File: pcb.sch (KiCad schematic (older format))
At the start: 1 part, among them U1 STM32F103C8Tx

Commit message: added correct MCU footprint and symbol
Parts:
- removed U1: STM32F103C8Tx, Package_QFP:LQFP-48_7x7mm_P0.5mm, symbol MCU_ST_STM32F1:STM32F103C8Tx
- added U1: STM32F103C8T6, STM32F103C8T6:QFP50P900X900X160-48N, symbol STM32F103C8T6:STM32F103C8T6
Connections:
- net labels added: +3.3VA, +3V3, GND, GNDA
- wire segments 0 -> 12
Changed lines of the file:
@@
 $EndDescr
 $Comp
-L MCU_ST_STM32F1:STM32F103C8Tx U1
-U 1 1 620F1E41
-P 6650 4100
-F 0 "U1" H 6600 2511 50  0000 C CNN
-F 1 "STM32F103C8Tx" H 6600 2420 50  0000 C CNN
-F 2 "Package_QFP:LQFP-48_7x7mm_P0.5mm" H 6050 2700 50  0001 R CNN
-F 3 "http://www.st.com/st-web-ui/static/active/en/resource/technical/document/datasheet/CD00161566.pdf" H 6650 4100 50  0001 C CNN
-	1    6650 4100
+L STM32F103C8T6:STM32F103C8T6 U1
+U 1 1 62107107
+P 7000 4600
+F 0 "U1" H 7000 6367 50  0000 C CNN
+F 1 "STM32F103C8T6" H 7000 6276 50  0000 C CNN
+F 2 "STM32F103C8T6:QFP50P900X900X160-48N" H 7000 4600 50  0001 L BNN
+F 3 "" H 7000 4600 50  0001 L BNN
+F 4 "10" H 7000 4600 50  0001 L BNN "PARTREV"
+F 5 "IPC7351B" H 7000 4600 50  0001 L BNN "STANDARD"
+F 6 "ST Microelectronics" H 7000 4600 50  0001 L BNN "MANUFACTURER"
+	1    7000 4600
 	1    0    0    -1
 $EndComp
+$Comp
+L power:+3V3 #PWR?
+U 1 1 6210956F
+P 8250 3000
+F 0 "#PWR?" H 8250 2850 50  0001 C CNN
+F 1 "+3V3" H 8265 3173 50  0000 C CNN
+F 2 "" H 8250 3000 50  0001 C CNN
+F 3 "" H 8250 3000 50  0001 C CNN
+	1    8250 3000
+	1    0    0    -1
+$EndComp
+Wire Wire Line
+	8250 3000 8250 3200
+Wire Wire Line
+	8250 3200 8000 3200
+$Comp
+L power:+3.3VA #PWR?
+U 1 1 6210AEB8
+P 8000 3000
+F 0 "#PWR?" H 8000 2850 50  0001 C CNN
+F 1 "+3.3VA" H 8015 3173 50  0000 C CNN
+F 2 "" H 8000 3000 50  0001 C CNN
+F 3 "" H 8000 3000 50  0001 C CNN
+	1    8000 3000
+	1    0    0    -1
+$EndComp
+Wire Wire Line
+	8000 3000 8000 3100
+$Comp
+L power:GND #PWR?
+U 1 1 6210B942
+P 8200 6050
+F 0 "#PWR?" H 8200 5800 50  0001 C CNN
+F 1 "GND" H 8205 5877 50  0000 C CNN
+F 2 "" H 8200 6050 50  0001 C CNN
+F 3 "" H 8200 6050 50  0001 C CNN
+	1    8200 6050
+	1    0    0    -1
+$EndComp
+$Comp
+L power:GNDA #PWR?
+U 1 1 6210C0B9
+P 8400 6050
+F 0 "#PWR?" H 8400 5800 50  0001 C CNN
+F 1 "GNDA" H 8405 5877 50  0000 C CNN
+F 2 "" H 8400 6050 50  0001 C CNN
+F 3 "" H 8400 6050 50  0001 C CNN
+	1    8400 6050
+	1    0    0    -1
+$EndComp
+Wire Wire Line
+	8200 6050 8200 6000
+Wire Wire Line
+	8200 6000 8000 6000
+Wire Wire Line
+	8400 6050 8400 5900
+Wire Wire Line
+	8400 5900 8000 5900
+Wire Wire Line
+	8250 3200 8500 3200
+Wire Wire Line
+	8500 3200 8500 2750
+Wire Wire Line
+	8500 2750 5950 2750
+Wire Wire Line
+	5950 2750 5950 3400
+Wire Wire Line
+	5950 3400 6000 3400
+Connection ~ 8250 3200
 $EndSCHEMATC

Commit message: created footprints and symbols for gps, compass and encoder
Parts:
- added G1: GPS_NEO_6M_module, components_ece445:GPS_NEO_6M_module, symbol components_senior_design:GPS_NEO_6M_module
- added U2: Shaft_encoder, components_ece445:shaft_encoder, symbol components_senior_design:Shaft_encoder
- added U3: compass_accelerometer, components_ece445:compass_accelerometer, symbol components_senior_design:compass_accelerometer
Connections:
- net labels added: +5V
- net labels removed: +3.3VA, GNDA
- wire segments 12 -> 22
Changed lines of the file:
@@
 $EndDescr
+$Comp
+L power:+3V3 #PWR03
+U 1 1 6210956F
+P 8250 3000
+F 0 "#PWR03" H 8250 2850 50  0001 C CNN
+F 1 "+3V3" H 8265 3173 50  0000 C CNN
+F 2 "" H 8250 3000 50  0001 C CNN
+F 3 "" H 8250 3000 50  0001 C CNN
+	1    8250 3000
+	1    0    0    -1
+$EndComp
+Wire Wire Line
+	8250 3000 8250 3200
+$Comp
+L power:GND #PWR02
+U 1 1 6210B942
+P 8200 6050
+F 0 "#PWR02" H 8200 5800 50  0001 C CNN
+F 1 "GND" H 8205 5877 50  0000 C CNN
+F 2 "" H 8200 6050 50  0001 C CNN
+F 3 "" H 8200 6050 50  0001 C CNN
+	1    8200 6050
+	1    0    0    -1
+$EndComp
+Wire Wire Line
+	8200 6050 8200 6000
+Wire Wire Line
+	8250 3200 8500 3200
+Wire Wire Line
+	8500 3200 8500 2750
+Wire Wire Line
+	8500 2750 5950 2750
+Wire Wire Line
+	5950 2750 5950 3400
+Wire Wire Line
+	5950 3400 6000 3400
+Connection ~ 8250 3200
+Wire Wire Line
+	8200 6000 8000 6000
 $Comp
 L STM32F103C8T6:STM32F103C8T6 U1
@@
 	1    0    0    -1
 $EndComp
+Wire Wire Line
+	8200 6000 8200 5900
+Connection ~ 8200 6000
+Wire Wire Line
+	8200 5900 8000 5900
 $Comp
-L power:+3V3 #PWR?
-U 1 1 6210956F
-P 8250 3000
-F 0 "#PWR?" H 8250 2850 50  0001 C CNN
-F 1 "+3V3" H 8265 3173 50  0000 C CNN
-F 2 "" H 8250 3000 50  0001 C CNN
-F 3 "" H 8250 3000 50  0001 C CNN
-	1    8250 3000
+L power:+3V3 #PWR0101
+U 1 1 6211EE7A
+P 3750 1750
+F 0 "#PWR0101" H 3750 1600 50  0001 C CNN
+F 1 "+3V3" H 3765 1923 50  0000 C CNN
+F 2 "" H 3750 1750 50  0001 C CNN
+F 3 "" H 3750 1750 50  0001 C CNN
+	1    3750 1750
+	1    0    0    -1
+$EndComp
+$Comp
+L power:GND #PWR0102
+U 1 1 6211F78C
+P 3750 2200
+F 0 "#PWR0102" H 3750 1950 50  0001 C CNN
+F 1 "GND" H 3755 2027 50  0000 C CNN
+F 2 "" H 3750 2200 50  0001 C CNN
+F 3 "" H 3750 2200 50  0001 C CNN
+	1    3750 2200
 	1    0    0    -1
 $EndComp
 Wire Wire Line
-	8250 3000 8250 3200
+	3400 2150 3750 2150
 Wire Wire Line
-	8250 3200 8000 3200
+	3750 2150 3750 2200
+Wire Wire Line
+	3400 1850 3750 1850
+Wire Wire Line
+	3750 1850 3750 1750
+Wire Wire Line
+	8000 3200 8100 3200
+Wire Wire Line
+	8000 3100 8100 3100
+Wire Wire Line
+	8100 3100 8100 3200
+Connection ~ 8100 3200
+Wire Wire Line
+	8100 3200 8250 3200
 $Comp
-L power:+3.3VA #PWR?
-U 1 1 6210AEB8
-P 8000 3000
-F 0 "#PWR?" H 8000 2850 50  0001 C CNN
-F 1 "+3.3VA" H 8015 3173 50  0000 C CNN
-F 2 "" H 8000 3000 50  0001 C CNN
-F 3 "" H 8000 3000 50  0001 C CNN
-	1    8000 3000
+L components_senior_design:GPS_NEO_6M_module G1
+U 1 1 621243D2
+P 3150 1900
+F 0 "G1" H 3208 2175 50  0000 C CNN
+F 1 "GPS_NEO_6M_module" H 3208 2084 50  0000 C CNN
+F 2 "components_ece445:GPS_NEO_6M_module" H 3150 1500 50  0001 C CNN
+F 3 "" H 3200 1950 50  0001 C CNN
+	1    3150 1900
+	1    0    0    -1
+$EndComp
+$Comp
+L components_senior_design:Shaft_encoder U2
+U 1 1 621258F0
+P 3150 2750
+F 0 "U2" H 3208 2975 50  0000 C CNN
+F 1 "Shaft_encoder" H 3208 2884 50  0000 C CNN
+F 2 "components_ece445:shaft_encoder" H 3200 2400 50  0001 C CNN
+F 3 "" H 3150 2950 50  0001 C CNN
+	1    3150 2750
+	1    0    0    -1
+$EndComp
+$Comp
+L power:+5V #PWR0103
+U 1 1 6212655A
+P 3650 2650
+F 0 "#PWR0103" H 3650 2500 50  0001 C CNN
+F 1 "+5V" H 3665 2823 50  0000 C CNN
+F 2 "" H 3650 2650 50  0001 C CNN
+F 3 "" H 3650 2650 50  0001 C CNN
+	1    3650 2650
 	1    0    0    -1
 $EndComp
 Wire Wire Line
-	8000 3000 8000 3100
+	3650 2650 3650 2750
+Wire Wire Line
+	3650 2750 3450 2750
 $Comp
-L power:GND #PWR?
-U 1 1 6210B942
-P 8200 6050
-F 0 "#PWR?" H 8200 5800 50  0001 C CNN
-F 1 "GND" H 8205 5877 50  0000 C CNN
-F 2 "" H 8200 6050 50  0001 C CNN
-F 3 "" H 8200 6050 50  0001 C CNN
-	1    8200 6050
-	1    0    0    -1
-$EndComp
-$Comp
-L power:GNDA #PWR?
-U 1 1 6210C0B9
-P 8400 6050
-F 0 "#PWR?" H 8400 5800 50  0001 C CNN
-F 1 "GNDA" H 8405 5877 50  0000 C CNN
-F 2 "" H 8400 6050 50  0001 C CNN
-F 3 "" H 8400 6050 50  0001 C CNN
-	1    8400 6050
+L power:GND #PWR0104
+U 1 1 62127216
+P 3650 3000
+F 0 "#PWR0104" H 3650 2750 50  0001 C CNN
+F 1 "GND" H 3655 2827 50  0000 C CNN
+F 2 "" H 3650 3000 50  0001 C CNN
+F 3 "" H 3650 3000 50  0001 C CNN
+	1    3650 3000
 	1    0    0    -1
 $EndComp
 Wire Wire Line
-	8200 6050 8200 6000
+	3450 2950 3650 2950
 Wire Wire Line
-	8200 6000 8000 6000
-Wire Wire Line
-	8400 6050 8400 5900
-Wire Wire Line
-	8400 5900 8000 5900
-Wire Wire Line
-	8250 3200 8500 3200
-Wire Wire Line
-	8500 3200 8500 2750
-Wire Wire Line
-	8500 2750 5950 2750
-Wire Wire Line
-	5950 2750 5950 3400
-Wire Wire Line
-	5950 3400 6000 3400
-Connection ~ 8250 3200
+	3650 2950 3650 3000
+$Comp
+L components_senior_design:compass_accelerometer U3
+U 1 1 6212A98F
+P 3200 3500
+F 0 "U3" H 3233 3715 50  0000 C CNN
+F 1 "compass_accelerometer" H 3233 3624 50  0000 C CNN
+F 2 "components_ece445:compass_accelerometer" H 3250 2550 50  0001 C CNN
+F 3 "" H 3200 3700 50  0001 C CNN
+	1    3200 3500
+	1    0    0    -1
+$EndComp
 $EndSCHEMATC

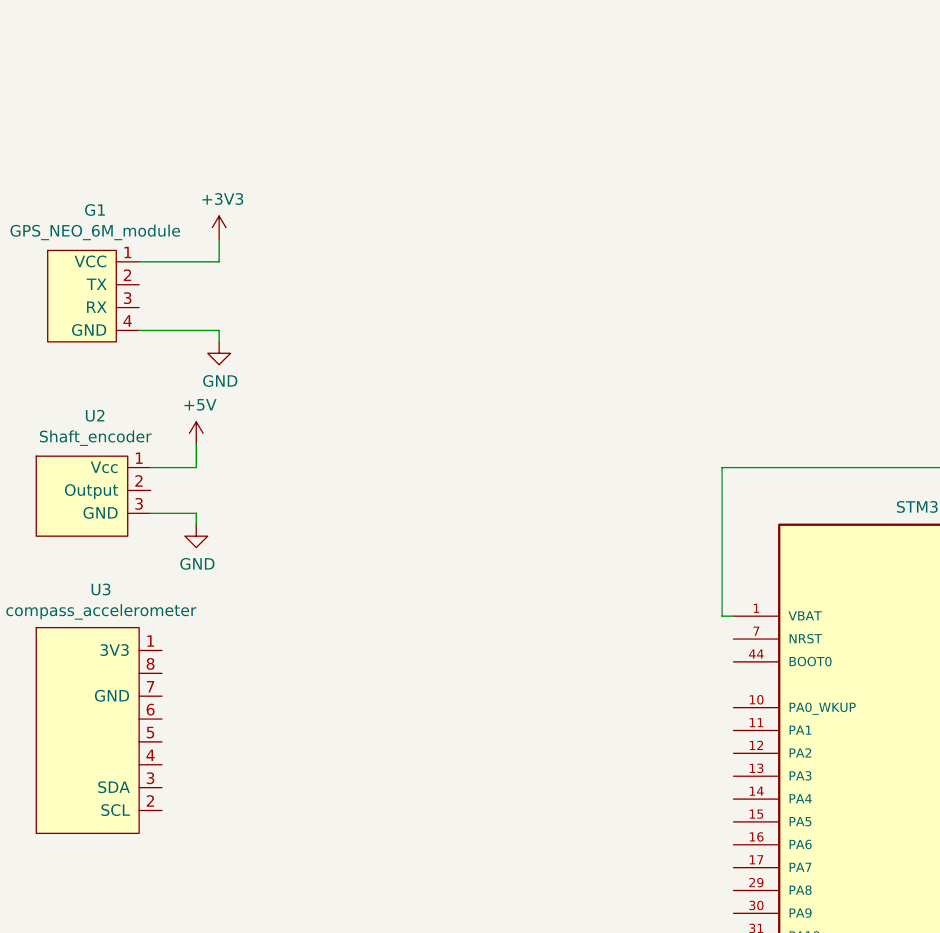
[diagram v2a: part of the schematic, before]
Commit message: added 3V7 to 3V3 convertor
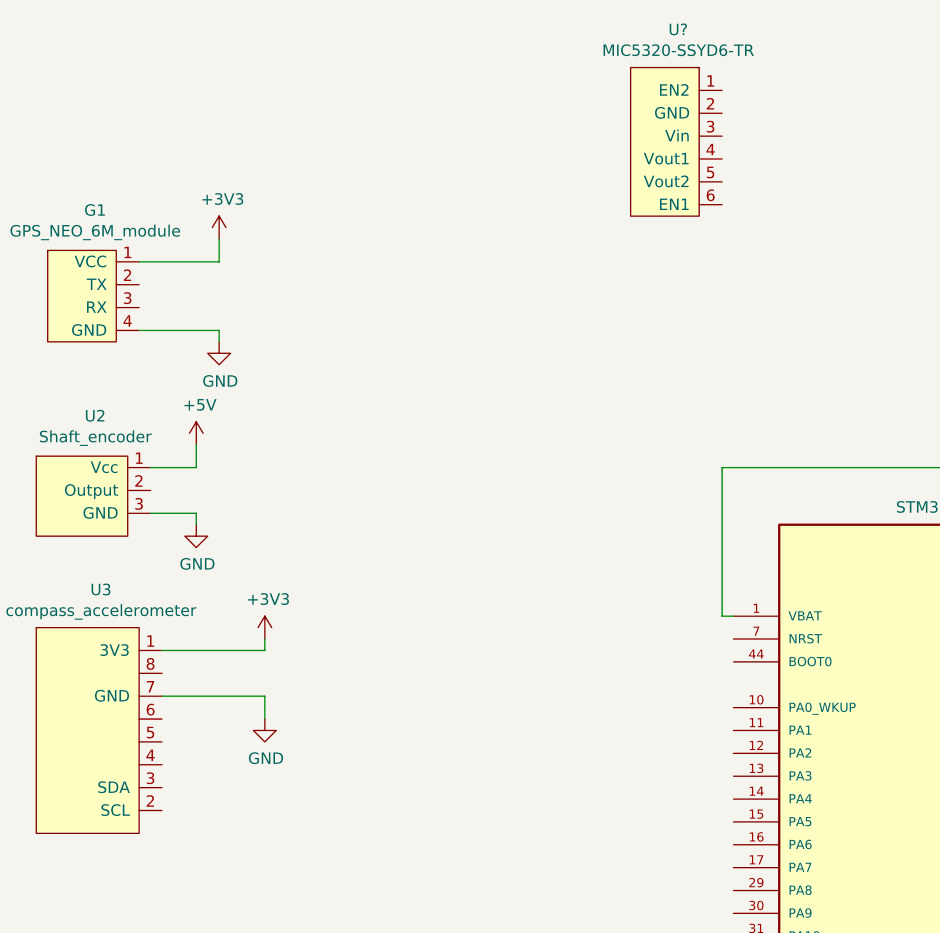
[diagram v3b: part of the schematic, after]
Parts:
- added U?: MIC5320-SSYD6-TR, MIC5320-SSYD6-TR:SOT95P280X110-6N, symbol components_senior_design:MIC5320-SSYD6-TR
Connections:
- net +3V3: now also U3.1 (3V3)
- net GND: now also U3.7 (GND)
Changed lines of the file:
@@
+	1    0    0    -1
+$EndComp
+$Comp
+L power:+3V3 #PWR0105
+U 1 1 6212C9CF
+P 3950 3500
+F 0 "#PWR0105" H 3950 3350 50  0001 C CNN
+F 1 "+3V3" H 3965 3673 50  0000 C CNN
+F 2 "" H 3950 3500 50  0001 C CNN
+F 3 "" H 3950 3500 50  0001 C CNN
+	1    3950 3500
+	1    0    0    -1
+$EndComp
+Wire Wire Line
+	3500 3550 3950 3550
+Wire Wire Line
+	3950 3550 3950 3500
+$Comp
+L power:GND #PWR0106
+U 1 1 6212D678
+P 3950 3850
+F 0 "#PWR0106" H 3950 3600 50  0001 C CNN
+F 1 "GND" H 3955 3677 50  0000 C CNN
+F 2 "" H 3950 3850 50  0001 C CNN
+F 3 "" H 3950 3850 50  0001 C CNN
+	1    3950 3850
+	1    0    0    -1
+$EndComp
+Wire Wire Line
+	3500 3750 3950 3750
+Wire Wire Line
+	3950 3750 3950 3850
+$Comp
+L components_senior_design:MIC5320-SSYD6-TR U?
+U 1 1 6213371B
+P 5750 1250
+F 0 "U?" H 5758 1665 50  0000 C CNN
+F 1 "MIC5320-SSYD6-TR" H 5758 1574 50  0000 C CNN
+F 2 "MIC5320-SSYD6-TR:SOT95P280X110-6N" H 5800 750 50  0001 C CNN
+F 3 "" H 5750 1200 50  0001 C CNN
+	1    5750 1250
 	1    0    0    -1
 $EndComp

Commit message: finished power supply
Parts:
- added C1, C2: 1uF, symbol device:C
- added J1: Conn_01x02, symbol Connector_Generic:Conn_01x02
- added U5: 3v7_to_5V_boost, components_ece445:3v7_to_5V_boost, symbol components_senior_design:3v7_to_5V_boost
- gave numbers to parts that had none: 1
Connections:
- net +3V3: now also U4.4 (Vout1), U4.5 (Vout2), C2.1
- net +5V: now also U4.1 (EN2), U4.3 (Vin), U4.6 (EN1), C1.1, U5.6 (Vout)
- net GND: now also U4.2 (GND), C1.2, C2.2, J1.2 (Pin_2), U5.3 (GND), U5.5 (GND)
- new net +3V8: J1.1 (Pin_1), U5.4 (Vbat)
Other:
- moved on the sheet: G1, U1, U2, U3, U4

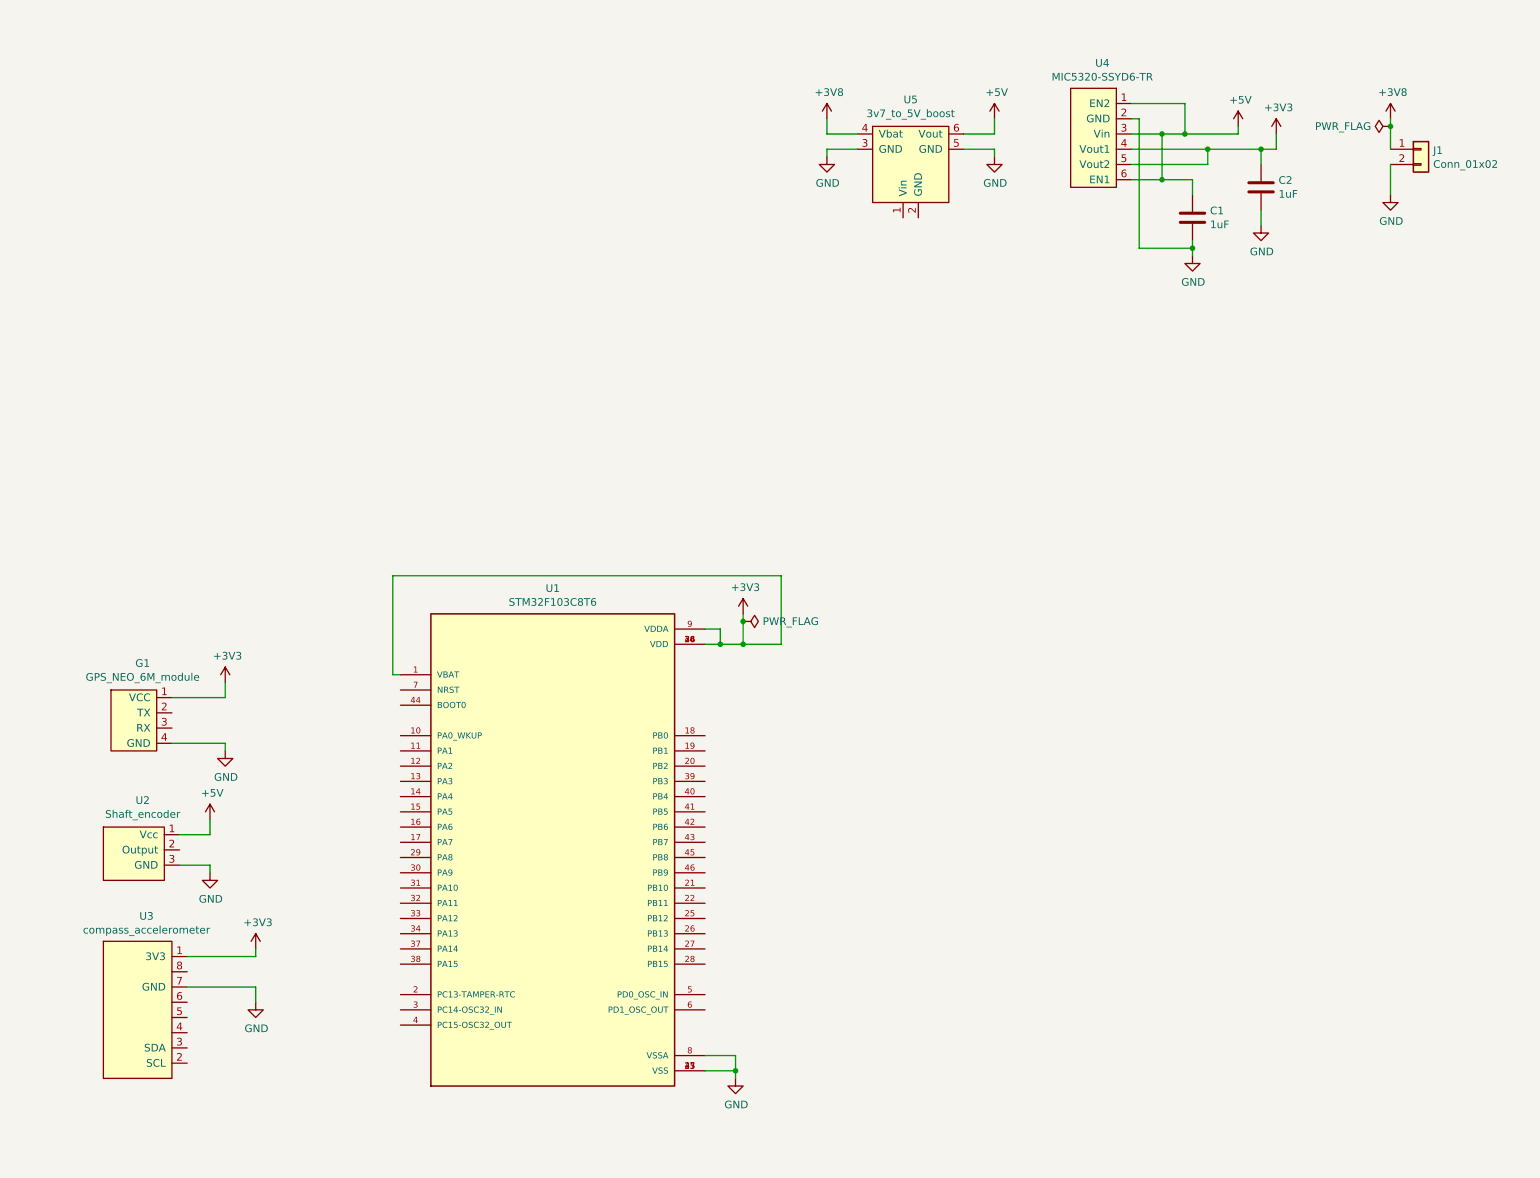
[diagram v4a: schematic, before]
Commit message: changed 3v3 regulator
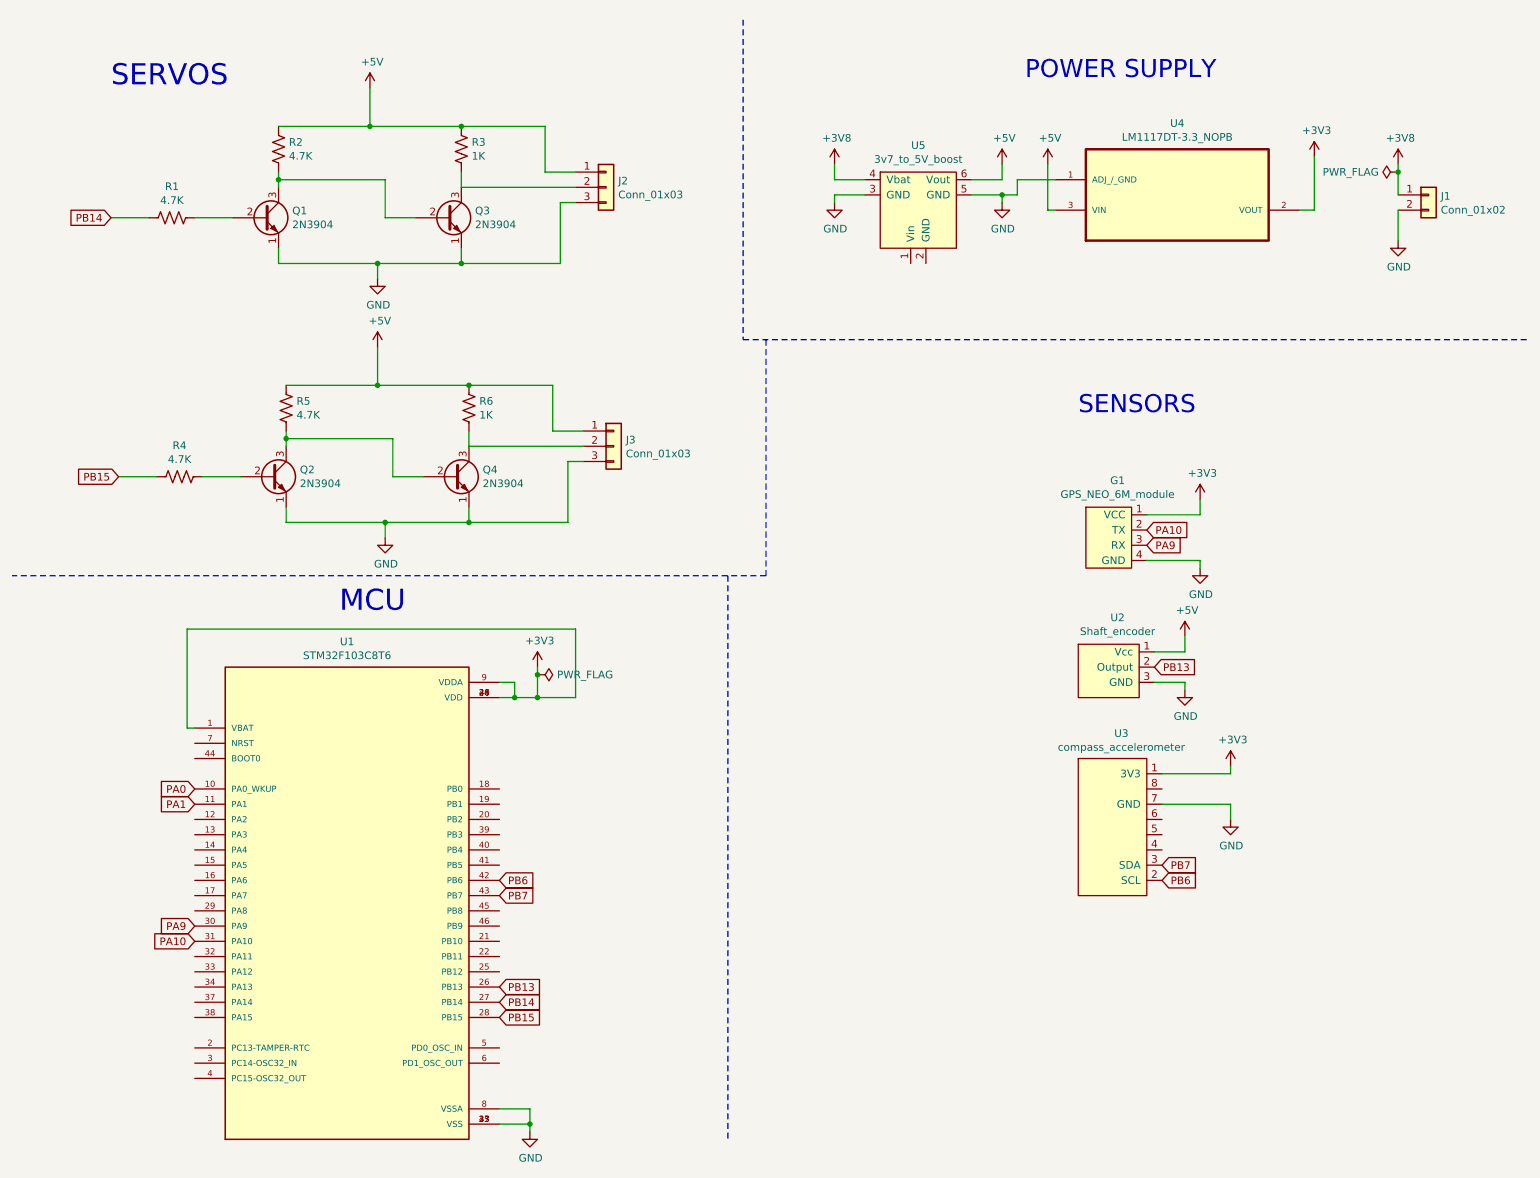
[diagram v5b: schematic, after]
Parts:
- removed C1, C2: 1uF, symbol device:C
- removed U4: MIC5320-SSYD6-TR, MIC5320-SSYD6-TR:SOT95P280X110-6N, symbol components_senior_design:MIC5320-SSYD6-TR
- added J2, J3: Conn_01x03, symbol Connector_Generic:Conn_01x03
- added Q1, Q2, Q3, Q4: 2N3904, Package_TO_SOT_THT:TO-92_Inline, symbol Transistor_BJT:2N3904
- added R1, R2, R4, R5: 4.7K, symbol device:R_US
- added R3, R6: 1K, symbol device:R_US
- added U4: LM1117DT-3.3_NOPB, LM1117DT-3_1:TO228P970X238-3N, symbol LM1117DT-3.3_NOPB:LM1117DT-3.3_NOPB
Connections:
- net +3V3: now also U4.2 (VOUT)
- net +5V: now also J2.1 (Pin_1), J3.1 (Pin_1), R2.1, R3.1, R5.1, R6.1, U4.3 (VIN)
- net GND: now also J2.3 (Pin_3), J3.3 (Pin_3), Q1.1 (E), Q2.1 (E), Q3.1 (E), Q4.1 (E), U4.1 (ADJ_/_GND)
- net PA0: now reaches U1.10 (PA0_WKUP)
- net PA1: now reaches U1.11 (PA1)
- net PB13: now reaches U1.26 (PB13)
- net PB13: now also U2.2 (Output)
- net PB14: now reaches U1.27 (PB14)
- net PB14: now also R1.2
- net PB15: now reaches U1.28 (PB15)
- net PB15: now also R4.2
- net PA9: now reaches U1.30 (PA9)
- net PA9: now also G1.3 (RX)
- net PA10: now reaches U1.31 (PA10)
- net PA10: now also G1.2 (TX)
- net PB6: now reaches U1.42 (PB6)
- net PB6: now also U3.2 (SCL)
- net PB7: now reaches U1.43 (PB7)
- net PB7: now also U3.3 (SDA)
- new net: Q1.2 (B), R1.1
- new net: Q1.3 (C), Q3.2 (B), R2.2
- new net: J2.2 (Pin_2), Q3.3 (C), R3.2
- new net: Q2.2 (B), R4.1
- new net: Q2.3 (C), Q4.2 (B), R5.2
- new net: J3.2 (Pin_2), Q4.3 (C), R6.2
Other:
- note added: "MCU"
- note added: "POWER SUPPLY"
- note added: "SENSORS"
- note added: "SERVOS"
- moved on the sheet: G1, J1, U1, U2, U3, U5
